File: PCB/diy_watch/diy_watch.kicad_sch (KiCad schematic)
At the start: 19 parts, among them P1 USB_C_Plug_USB2.0, SW1 SW_Push, U1 W25Q32JVSS, U2 DS3231MZ, U3 RP2040, Y1 12MHz_crystal

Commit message: Adding datasheets
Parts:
- removed TP1, TP2, TP3: TestPoint, TestPoint:TestPoint_Pad_D1.0mm, symbol Connector:TestPoint
- added J1: Debug Port, Connector_PinHeader_2.54mm:PinHeader_1x03_P2.54mm_Vertical, symbol Connector:Conn_01x03_Pin
- added R2: R, Resistor_SMD:R_0402_1005Metric, symbol Device:R
- added U5: LTC4054ES5-4.2, Package_TO_SOT_SMD:TSOT-23-5, symbol Battery_Management:LTC4054ES5-4.2
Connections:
- net +3.3V: now also U2.2 (VCC)
- net GND: now also BT1.2 (-), U2.5 (GND), J1.2 (Pin_2), R2.2, U5.2 (GND)
- net at U3.24 (SWCLK): now also J1.1 (Pin_1)
- net COM1: now reaches U4.1 (COM1)
- net COM1: now also U3.2 (GPIO0)
- net F: now reaches U4.10 (F)
- net F: now also U3.12 (GPIO9)
- net G: now reaches U4.11 (G)
- net G: now also U3.13 (GPIO10)
- net H: now reaches U4.12 (H)
- net H: now also U3.14 (GPIO11)
- net I: now reaches U4.13 (I)
- net I: now also U3.15 (GPIO12)
- net J: now reaches U4.14 (J)
- net J: now also U3.16 (GPIO13)
- net K: now reaches U4.15 (K)
- net K: now also U3.17 (GPIO14)
- net L: now reaches U4.16 (L)
- net L: now also U3.18 (GPIO15)
- net COM2: now reaches U4.2 (COM2)
- net COM2: now also U3.3 (GPIO1)
- net COM3: now reaches U4.3 (COM3)
- net COM3: now also U3.4 (GPIO2)
- net COM4: now reaches U4.4 (COM4)
- net COM4: now also U3.5 (GPIO3)
- net A: now reaches U4.5 (A)
- net A: now also U3.6 (GPIO4)
- net B: now reaches U4.6 (B)
- net B: now also U3.7 (GPIO5)
- net C: now reaches U4.7 (C)
- net C: now also U3.8 (GPIO6)
- net D: now reaches U4.8 (D)
- net D: now also U3.9 (GPIO7)
- net E: now reaches U4.9 (E)
- net E: now also U3.11 (GPIO8)
- net +BATT: now reaches BT1.1 (+)
- net +BATT: now also U2.6 (VBAT), U5.3 (BAT)
- net at U3.25 (SWD): now also J1.3 (Pin_3)
- net RTC_SCL: now reaches U3.27 (GPIO16)
- net RTC_SCL: now also U2.8 (SCL)
- net RTC_SDA: now reaches U3.28 (GPIO17)
- net RTC_SDA: now also U2.7 (SDA)
- net RTC_INT: now reaches U3.29 (GPIO18)
- net RTC_INT: now also U2.3 (~{INT}/SQW)
- net +3V3: now reaches U2.4 (~{RST})
- new net: R2.1, U5.5 (PROG)
- new net +5V: U5.4 (V_{CC})
- no-connect marks 0 -> 1
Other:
- note added: "Charging Circuit"
- note added: "LCD Display"
- note added: "RTC"
- moved on the sheet: BT1, U2

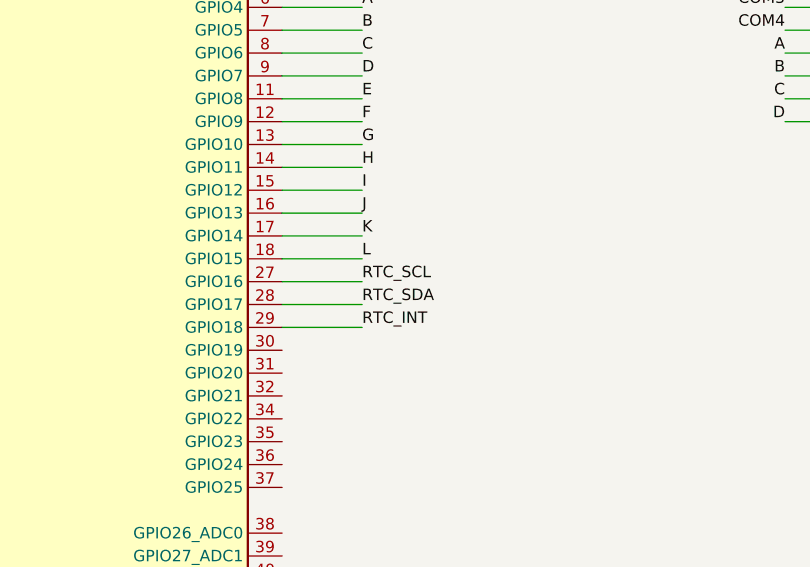
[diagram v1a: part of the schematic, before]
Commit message: Updating LCD driver Updated RTC pinout
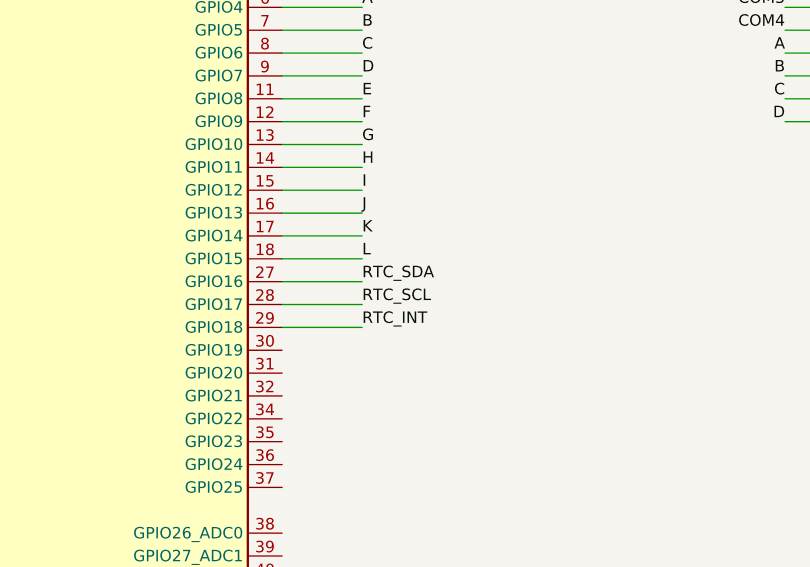
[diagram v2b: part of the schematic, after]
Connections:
- net RTC_SCL: now also U3.28 (GPIO17); no longer U3.27 (GPIO16)
- net RTC_SDA: now also U3.27 (GPIO16); no longer U3.28 (GPIO17)
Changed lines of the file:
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@@
     (effects (font (size 1.27 1.27)) (justify left bottom))
   )
-  (label "RTC_SCL" (at 137.16 101.6 0) (fields_autoplaced)
+  (label "RTC_SDA" (at 137.16 101.6 0) (fields_autoplaced)
     (effects (font (size 1.27 1.27)) (justify left bottom))
   )
-  (label "RTC_SDA" (at 137.16 104.14 0) (fields_autoplaced)
+  (label "RTC_SCL" (at 137.16 104.14 0) (fields_autoplaced)
     (effects (font (size 1.27 1.27)) (justify left bottom))
   )

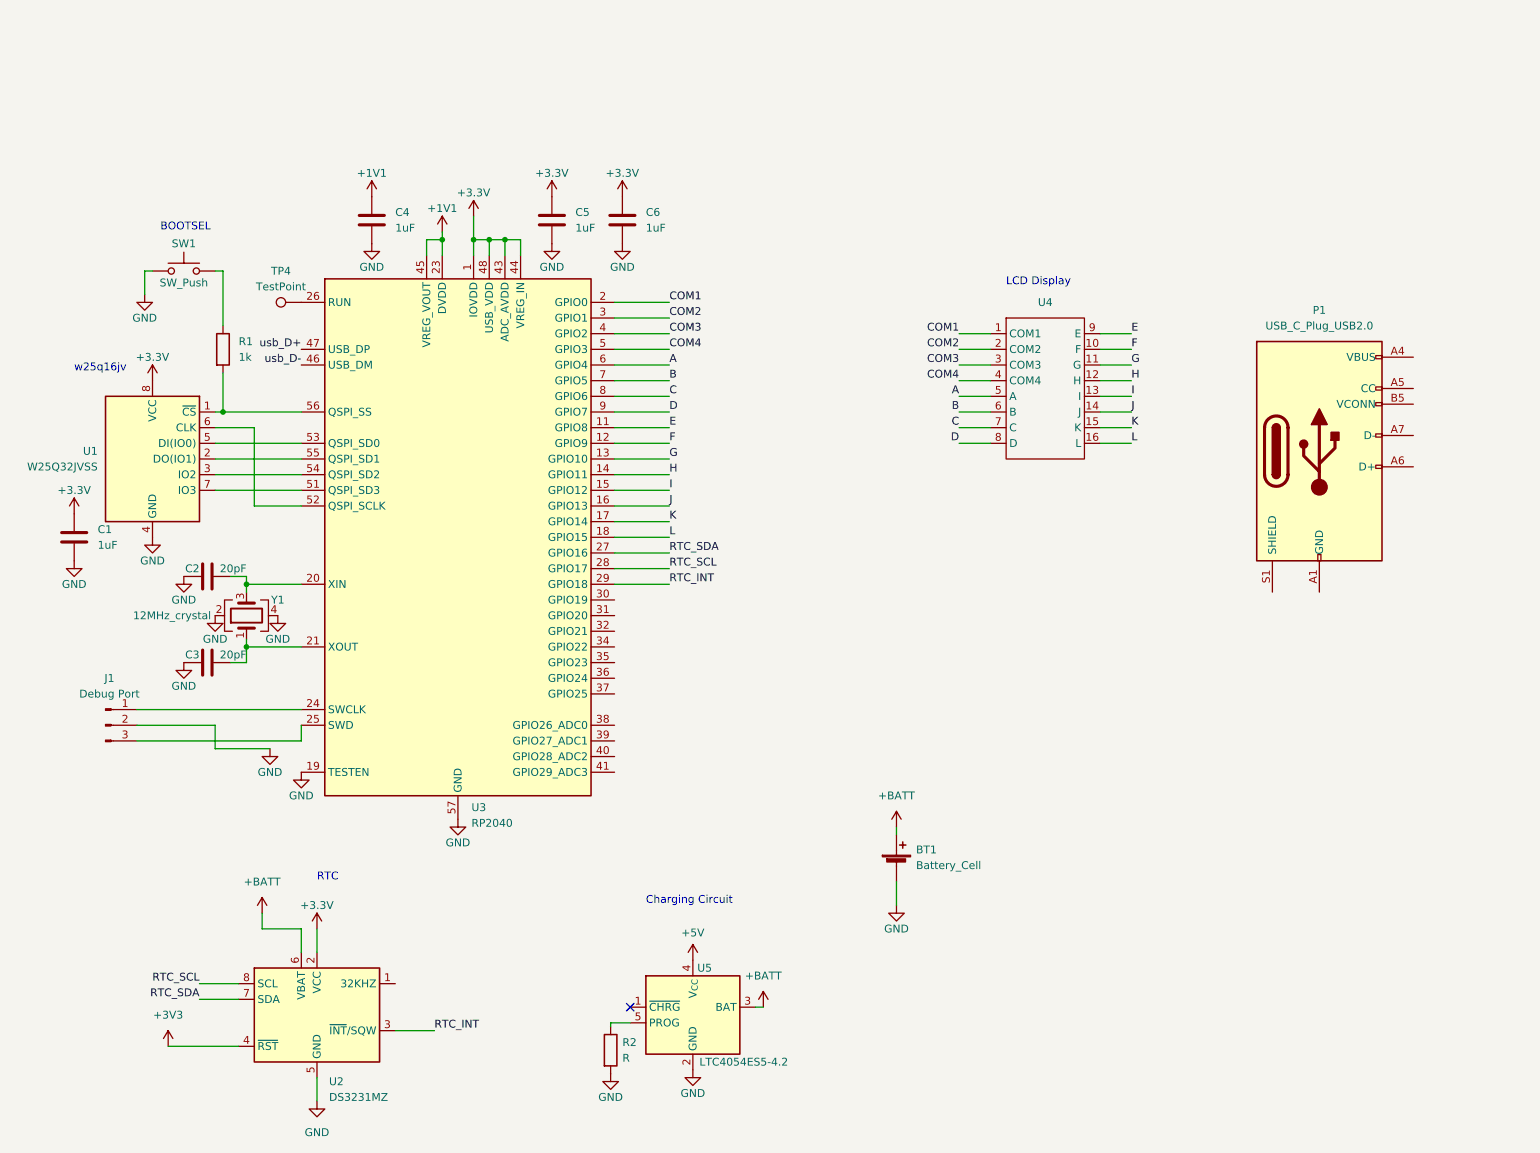
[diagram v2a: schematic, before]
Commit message: Updating watch PCB
Added COM resistor pullup/downs
Added switch
Added LEDs
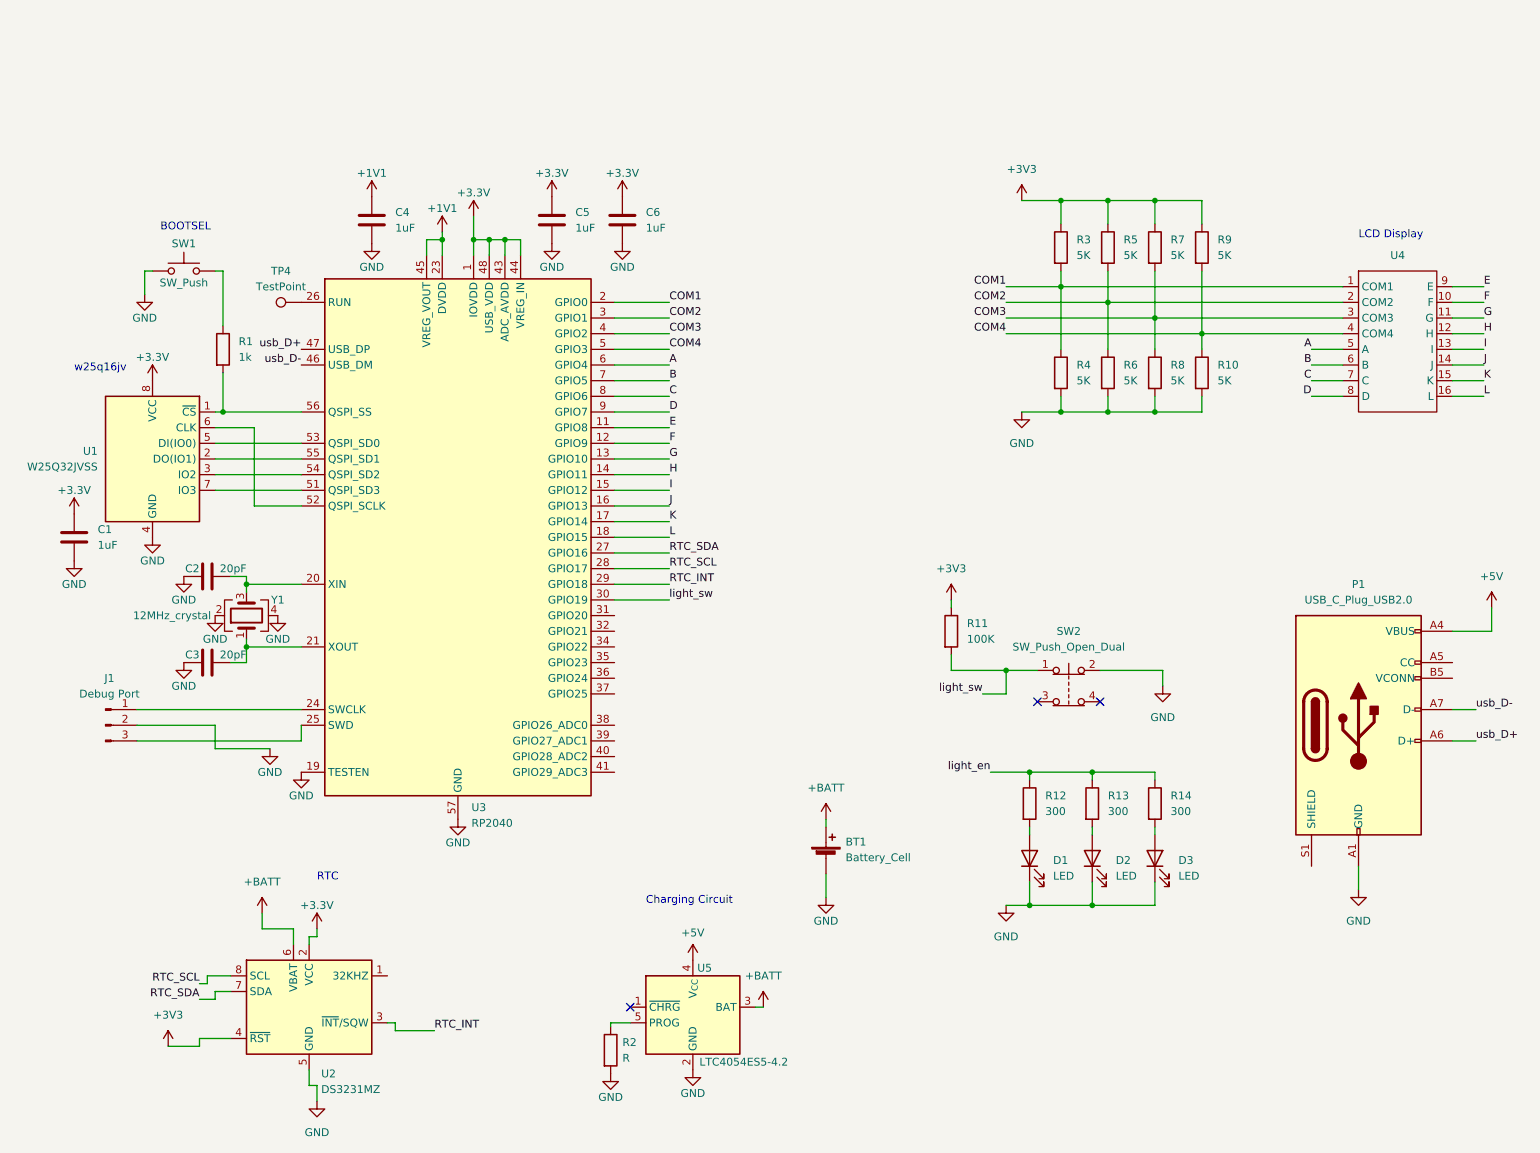
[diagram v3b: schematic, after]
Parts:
- added D1, D2, D3: LED, LED_SMD:LED_0805_2012Metric, symbol Device:LED
- added R10, R3, R4, R5, R6, R7, R8, R9: 5K, Resistor_SMD:R_0402_1005Metric, symbol Device:R
- added R11: 100K, symbol Device:R
- added R12, R13, R14: 300, LED_SMD:LED_0402_1005Metric, symbol Device:R
- added SW2: SW_Push_Open_Dual, symbol Switch:SW_Push_Open_Dual
- C1, C2, C3, C4, C5, C6: footprint Capacitor_SMD:C_0805_2012Metric -> Capacitor_SMD:C_0402_1005Metric
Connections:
- net +3V3: now also R11.1, R3.1, R5.1, R7.1, R9.1
- net +5V: now also P1.A4 (VBUS), P1.A9 (VBUS), P1.B4 (VBUS), P1.B9 (VBUS)
- net COM1: now also R3.2, R4.1
- net COM2: now also R5.2, R6.1
- net COM3: now also R7.2, R8.1
- net COM4: now also R10.1, R9.2
- net GND: now also P1.A1 (GND), P1.A12 (GND), P1.B1 (GND), P1.B12 (GND), D1.1 (K), D2.1 (K), D3.1 (K), R10.2, R4.2, R6.2, R8.2, SW2.2
- net usb_D+: now also P1.A6 (D+)
- net usb_D-: now also P1.A7 (D-)
- net light_sw: now reaches U3.30 (GPIO19)
- net light_sw: now also R11.2, SW2.1
- new net: D1.2 (A), R12.2
- new net: D2.2 (A), R13.2
- new net: D3.2 (A), R14.2
- new net light_en: R12.1, R13.1, R14.1
- no-connect marks 1 -> 3
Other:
- moved on the sheet: BT1, P1, U2, U4

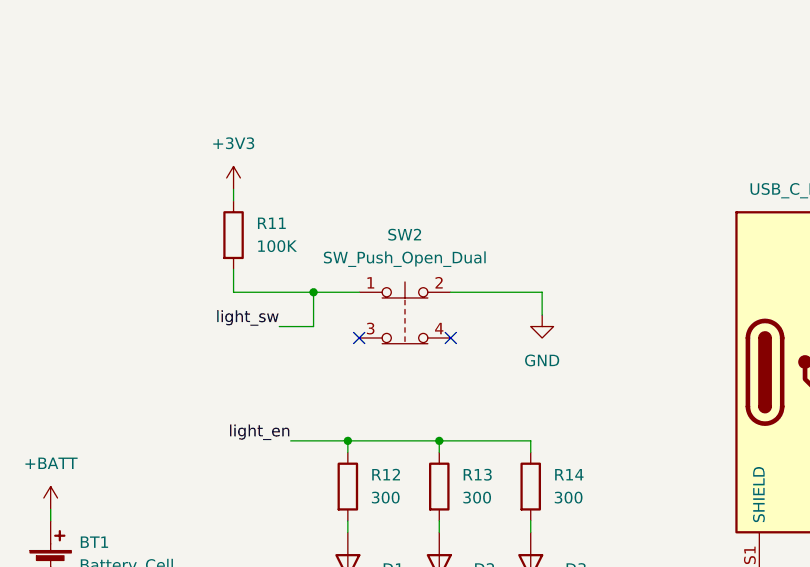
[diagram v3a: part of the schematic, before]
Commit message: Updated swich layout and symbol
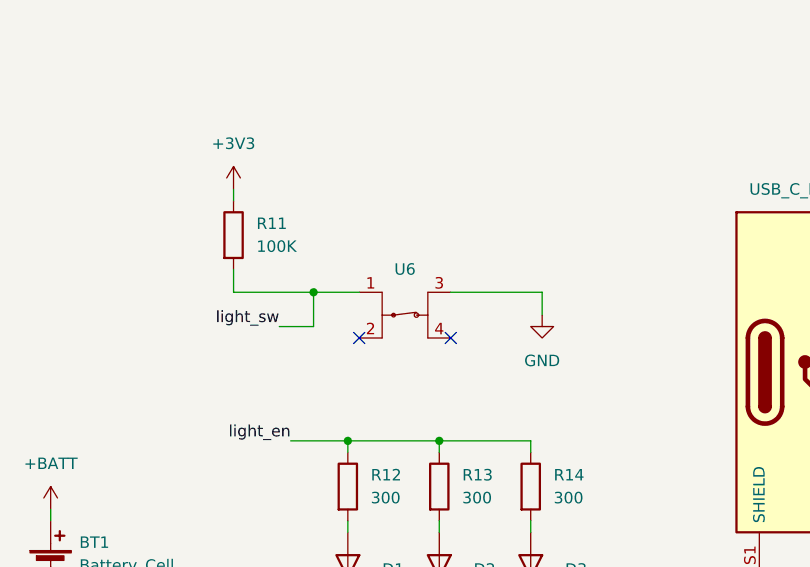
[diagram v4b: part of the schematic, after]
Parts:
- removed SW2: SW_Push_Open_Dual, symbol Switch:SW_Push_Open_Dual
- added U6: ~, DIY_Watch_lib:Diptronics FTE-3, symbol DIY_Watch_lib:Diptronics_FTE-3CA-V-T/R
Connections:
- net GND: now also U6.3
- net light_sw: now also U6.1
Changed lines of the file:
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@@
+    )
+  )
+  (symbol (lib_id "DIY_Watch_lib:Diptronics_FTE-3CA-V-T/R") (at 201.93 121.92 0) (unit 1)
+    (in_bom yes) (on_board yes) (dnp no) (fields_autoplaced)
+    (property "Reference" "U6" (at 201.93 118.11 0)
+      (effects (font (size 1.27 1.27)))
+    )
+    (property "Value" "~" (at 201.93 121.92 0)
+      (effects (font (size 1.27 1.27)))
+    )
+    (property "Footprint" "DIY_Watch_lib:Diptronics FTE-3" (at 201.93 121.92 0)
+      (effects (font (size 1.27 1.27)) hide)
+    )
+    (property "Datasheet" "" (at 201.93 121.92 0)
+      (effects (font (size 1.27 1.27)) hide)
+    )
+    (pin "1")
+    (pin "2")
+    (pin "3")
+    (pin "4")
+    (instances
+      (project "diy_watch"
+        (path "/12c7509a-2a16-4dc7-8785-00872e5a9f11"
+          (reference "U6") (unit 1)
+        )
+      )
     )
   )
@@
         )
       )
-    )
-  )
-  (symbol (lib_id "Switch:SW_Push_Open_Dual") (at 201.93 120.65 0) (unit 1)
-    (in_bom yes) (on_board yes) (dnp no) (fields_autoplaced)
-    (property "Reference" "SW2" (at 201.93 114.3 0)
-      (effects (font (size 1.27 1.27)))
-    )
-    (property "Value" "SW_Push_Open_Dual" (at 201.93 116.84 0)
-      (effects (font (size 1.27 1.27)))
-    )
-    (property "Footprint" "" (at 201.93 115.57 0)
-      (effects (font (size 1.27 1.27)) hide)
-    )
-    (property "Datasheet" "~" (at 201.93 115.57 0)
-      (effects (font (size 1.27 1.27)) hide)
-    )
-    (pin "1")
-    (pin "2")
-    (pin "3")
-    (pin "4")
-    (instances
-      (project "diy_watch"
-        (path "/12c7509a-2a16-4dc7-8785-00872e5a9f11"
-          (reference "SW2") (unit 1)
-        )
-      )

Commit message: Routed most of the PCB, big staggetti
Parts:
- removed J1: Debug Port, Connector_PinHeader_2.54mm:PinHeader_1x03_P2.54mm_Vertical, symbol Connector:Conn_01x03_Pin
- removed P1: USB_C_Plug_USB2.0, Connector_USB:USB_C_Receptacle_GCT_USB4110, symbol Connector:USB_C_Plug_USB2.0
- added J1: USB_B_Micro, Connector_USB:USB_Micro-B_GCT_USB3076-30-A, symbol Connector:USB_B_Micro
- added TP1: TP_SWCLK, TestPoint:TestPoint_Pad_D1.5mm, symbol Connector:TestPoint
- added TP2: TP_GND, TestPoint:TestPoint_Pad_D1.5mm, symbol Connector:TestPoint
- added TP3: TP_SWD, TestPoint:TestPoint_Pad_D1.5mm, symbol Connector:TestPoint
- added TP5: TP_3V3, TestPoint:TestPoint_Pad_D1.5mm, symbol Connector:TestPoint
- added U7: XC6210B332MR, Package_TO_SOT_SMD:SOT-23-5, symbol Regulator_Linear:XC6210B332MR
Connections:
- net +3V3 is gone; now on net +3.3V: R11.1, R3.1, R5.1, R7.1, R9.1, U2.4 (~{RST})
- net +3.3V: now also TP5.1, U7.5 (VOUT)
- net +5V: now also J1.1 (VBUS)
- net +BATT: now also U7.1 (VIN)
- net GND: now also J1.5 (GND), J1.6 (Shield), TP2.1, U7.2 (GND)
- net light_en: now also U3.31 (GPIO20)
- net usb_D+: now also J1.3 (D+)
- net usb_D-: now also J1.2 (D-)
- net at U3.24 (SWCLK): now also TP1.1
- net at U3.25 (SWD): now also TP3.1
- no-connect marks 3 -> 4
